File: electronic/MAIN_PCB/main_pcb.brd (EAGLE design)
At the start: 53 x 77.5 mm, 14 parts, among them J5 D1, J6 D2, J7 UART3, J8 UART1, T1 2N2222

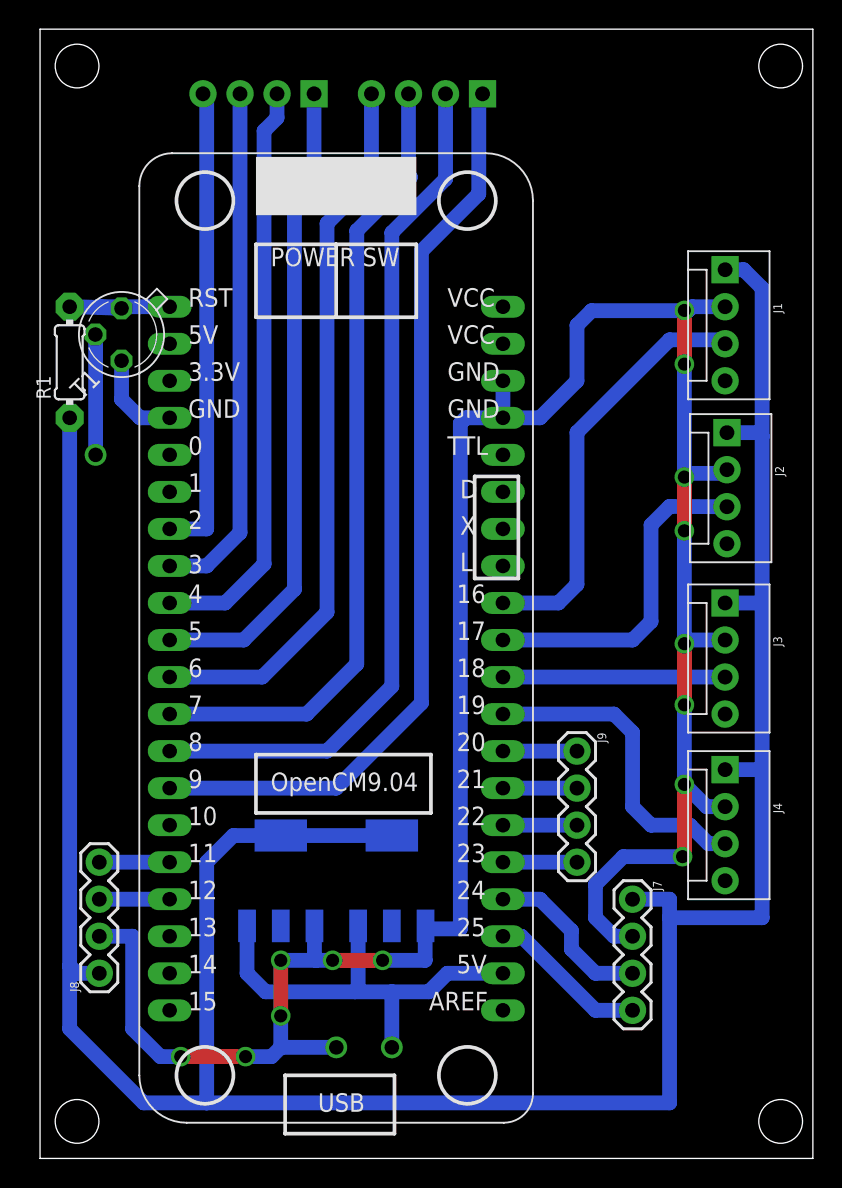
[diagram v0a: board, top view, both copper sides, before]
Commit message: add power commutator
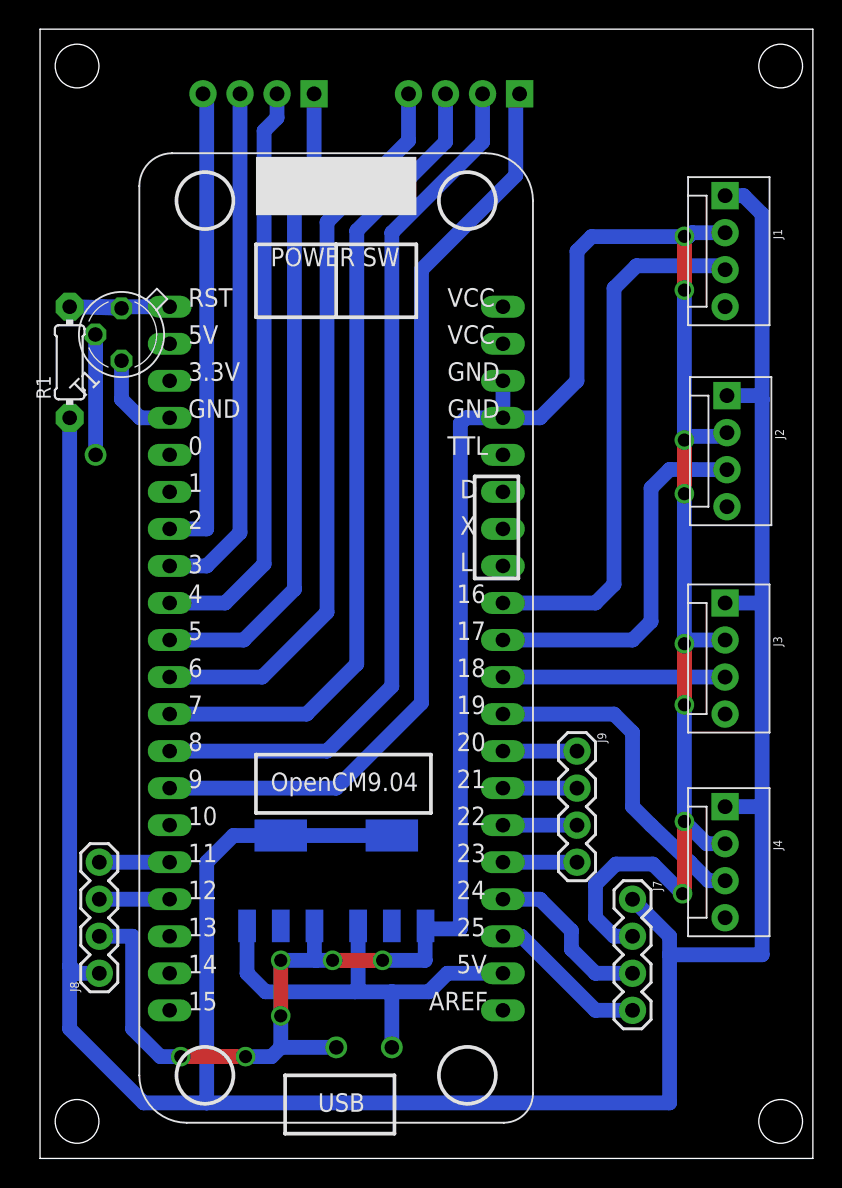
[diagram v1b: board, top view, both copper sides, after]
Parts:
- moved J1 5.08 mm to (41.9, 66.0)
- moved J4 2.54 mm to (41.9, 24.1)
- moved J2 2.54 mm to (42.0, 52.3)
- moved J6 2.54 mm to (27.8, 73.0)
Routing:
- net GND: track 173.4 -> 186.8 mm
- net E1: track 28.9 -> 36.8 mm
- net +3V3: track 194.1 -> 200.2 mm
- net E2: track 23.0 -> 25.6 mm
- net N$6: track 49.5 -> 50.5 mm
- net N$9: track 63.2 -> 64.3 mm
- net N$8: track 59.2 -> 60.3 mm
- net E4: track 21.9 -> 22.9 mm
- net N$7: track 54.9 -> 55.9 mm
